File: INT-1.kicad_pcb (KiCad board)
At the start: 2 copper layers, 53 parts, among them SW1 SW_Push, U1 ATmega32U2-MU, U2 PRTR5V0U2X, Y1 Crystal_GND24_Small

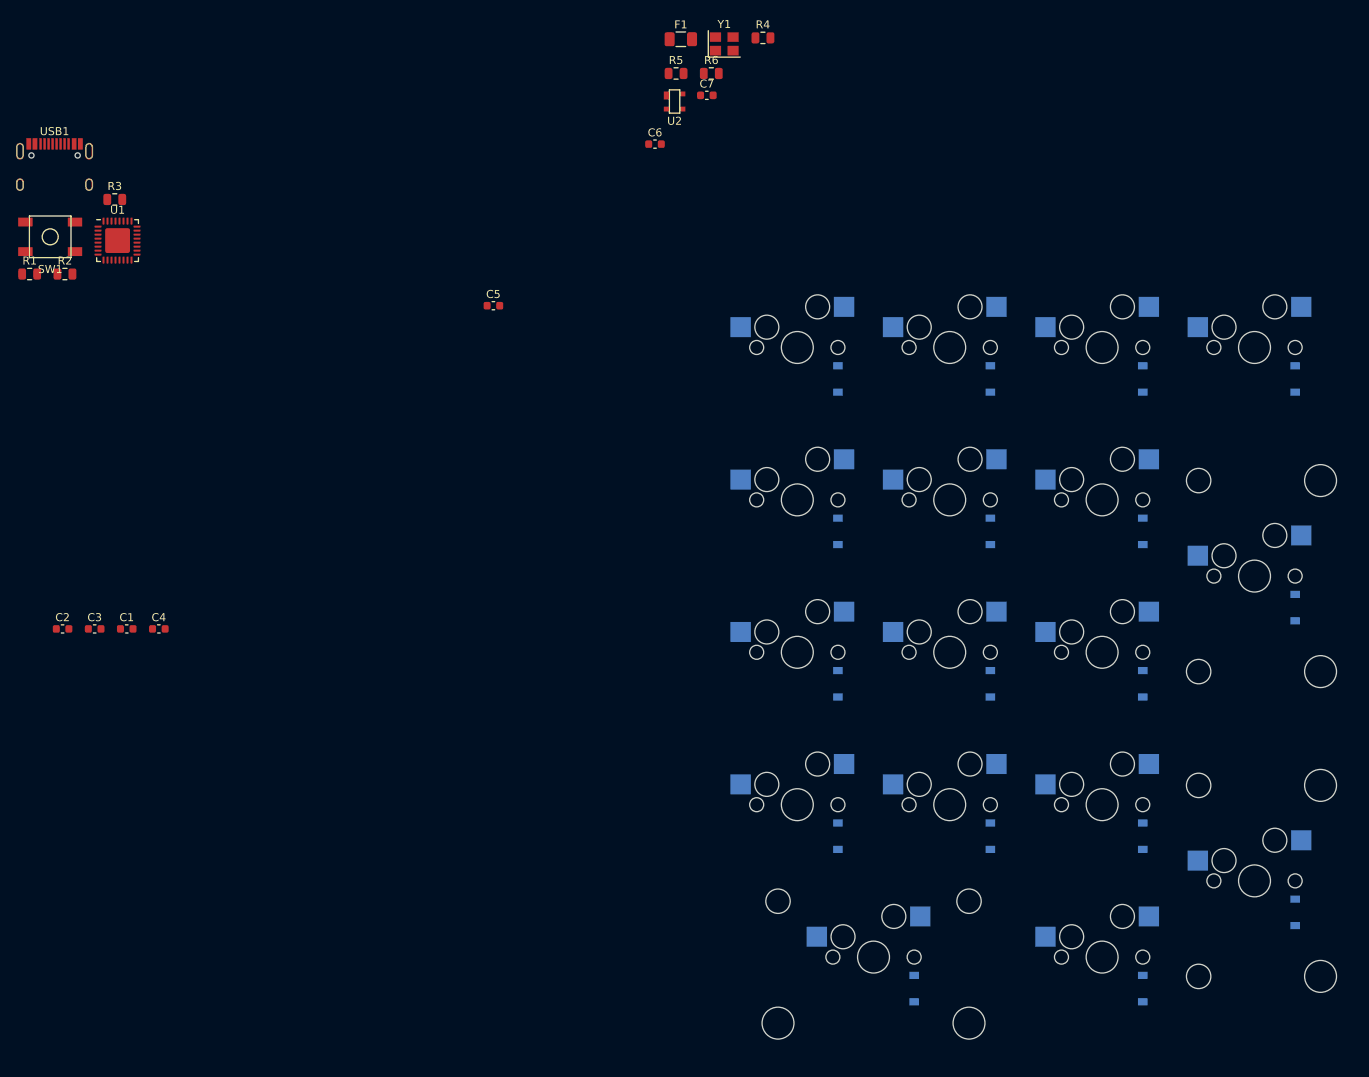
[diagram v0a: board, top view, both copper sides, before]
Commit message: Finished edge cuts
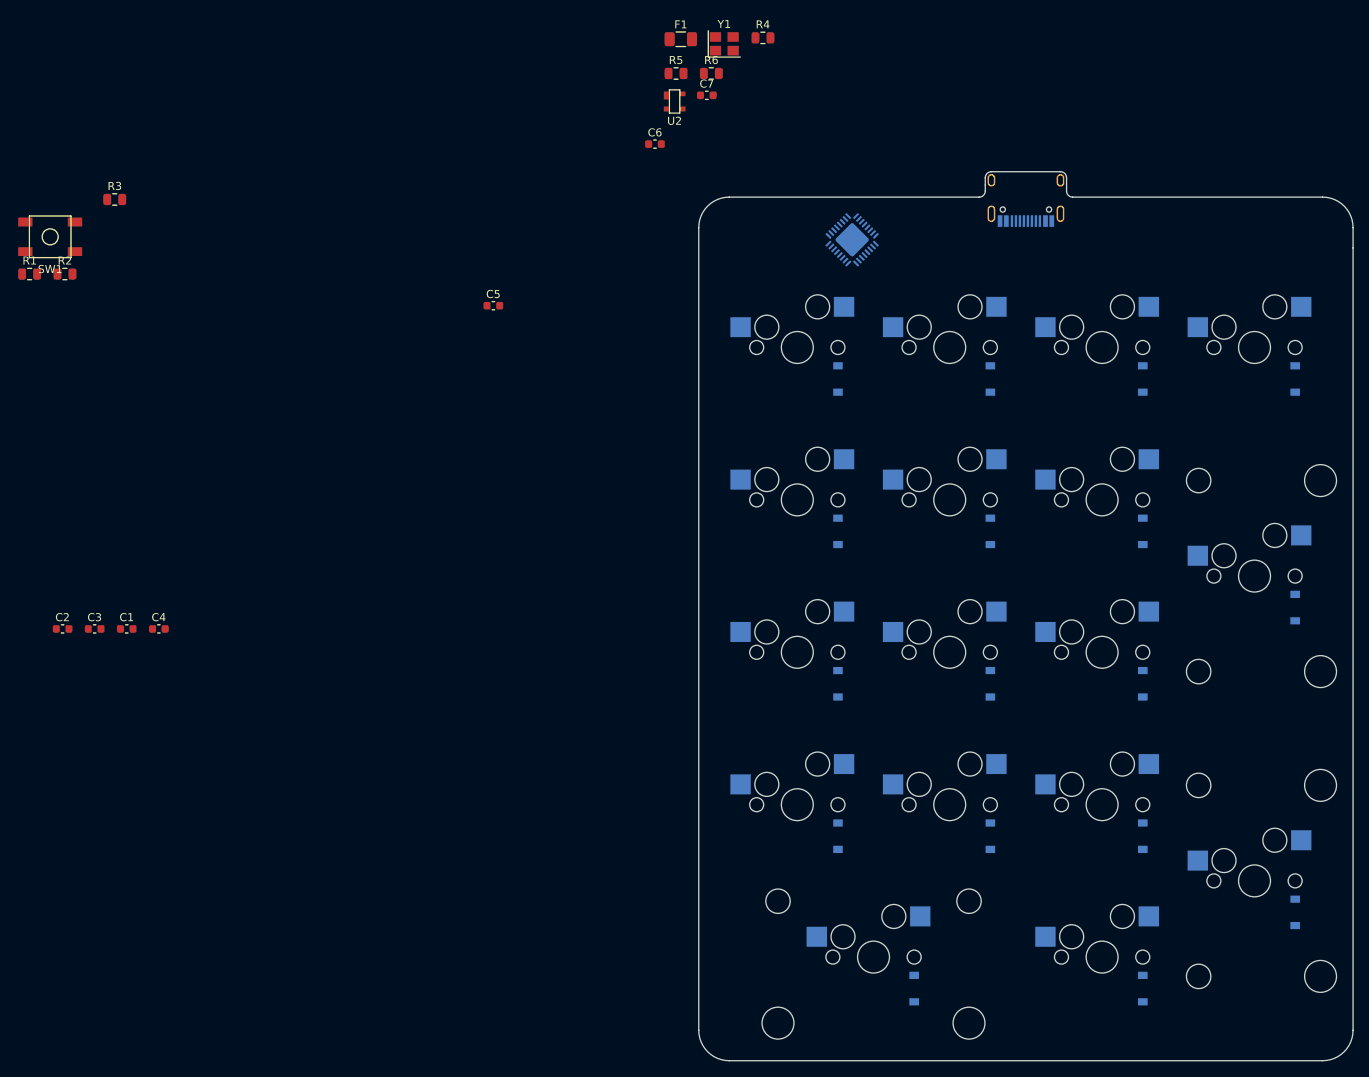
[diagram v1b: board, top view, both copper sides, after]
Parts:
- U1, USB1: moved to B.Cu
- moved USB1 121.6 mm to (152.1, 33.4)
- moved U1 91.8 mm to (130.4, 43.4), turned to 135 degrees
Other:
- board outline added: 81.8 x 111.1 mm

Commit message: Finished trace routing
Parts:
- removed C7: 0.1uF, Capacitor_SMD:C_0603_1608Metric
- C1, C2, C3, C5, C6, F1, R1, R2, R3, R4, R5, R6, SW1, U2, Y1: moved to B.Cu
- C4: value 10uF -> 4.7uF; moved to B.Cu
- moved C4 130.1 mm to (165.2, 45.5)
- moved C2 117.2 mm to (140.5, 48.4)
- moved R3 113.2 mm to (151.1, 47.5), turned to 90 degrees
- moved C1 113.1 mm to (140.6, 40.8), turned to 180 degrees
- moved C3 108.9 mm to (130.9, 39.1)
- moved R2 102.1 mm to (134.1, 48.8), turned to 180 degrees
- moved R1 100.6 mm to (127.9, 40.2), turned to 270 degrees
- moved SW1 91.0 mm to (121.2, 42.7), turned to 270 degrees
- moved C5 80.2 mm to (165.2, 42.5)
- moved C6 60.0 mm to (165.2, 39.6)
- moved F1 56.8 mm to (159.8, 43.8), turned to 90 degrees
- moved R6 48.1 mm to (155.7, 44.5), turned to 90 degrees
- moved U2 47.4 mm to (152.1, 44.1), turned to 180 degrees
- moved R5 45.6 mm to (148.6, 44.3), turned to 90 degrees
- moved R4 44.8 mm to (153.2, 47.5), turned to 90 degrees
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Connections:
- U1 pad 14: COL0 -> Net-(U1-Pad14)
- U1 pad 15: COL1 -> COL3
- U1 pad 16: COL2 -> ROW0
- U1 pad 17: COL3 -> ROW1
- U1 pad 18: ROW0 -> ROW2
- U1 pad 19: ROW1 -> COL2
- U1 pad 20: ROW2 -> COL1
- U1 pad 21: ROW3 -> COL0
- U1 pad 22: Net-(U1-Pad22) -> ROW3
- U1 pad 23: Net-(U1-Pad23) -> ROW4
- U1 pad 5: ROW4 -> Net-(U1-Pad5)
- U2 pad 2: Net-(R3-Pad2) -> Net-(R4-Pad2)
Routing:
- net COL2: track 0.00 -> 202.6 mm, vias 0 -> 5
- net ROW4: track 0.00 -> 185.7 mm
- net COL0: track 0.00 -> 166.5 mm, vias 0 -> 5
- net COL1: track 0.00 -> 164.1 mm, vias 0 -> 4
- net ROW3: track 0.00 -> 141.7 mm
- net ROW2: track 0.00 -> 141.3 mm
- net COL3: track 0.00 -> 129.2 mm, vias 0 -> 3
- net GND: track 0.00 -> 102.9 mm, vias 0 -> 2
- net ROW1: track 0.00 -> 98.5 mm
- net ROW0: track 0.00 -> 74.0 mm
- net +5V: track 0.00 -> 60.3 mm, vias 0 -> 4
- net D+: track 0.00 -> 37.4 mm, vias 0 -> 2
- net D-: track 0.00 -> 35.9 mm, vias 0 -> 2
- net VCC: track 0.00 -> 16.2 mm, vias 0 -> 3
- net Net-(R1-Pad2): track 0.00 -> 12.9 mm
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- added copper zone on B.Cu, net GND
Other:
- net class Power: trace_width 0.381 -> 0.25

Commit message: Added mounting holes
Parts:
- added REF**: Generic-Mounthole, random-keyboard-parts:Generic-Mounthole, F.Cu at (114.7, 142.9)
- added REF**: Generic-Mounthole, random-keyboard-parts:Generic-Mounthole, F.Cu at (189.5, 142.9)
- added REF**: Generic-Mounthole, random-keyboard-parts:Generic-Mounthole, F.Cu at (189.5, 41.3)
- added REF**: Generic-Mounthole, random-keyboard-parts:Generic-Mounthole, F.Cu at (114.7, 41.3)
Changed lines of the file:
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@@
     (tracks 442)
     (zones 0)
-    (modules 52)
+    (modules 56)
     (nets 54)
   )
@@
     (add_net VCC)
   )
+  (module random-keyboard-parts:Generic-Mounthole (layer F.Cu)
+    (at 114.681 142.875)
+    (attr virtual)
+    (fp_text reference REF** (at 0 2) (layer Dwgs.User)
+      (effects (font (size 1 1) (thickness 0.15)))
+    )
+    (fp_text value Generic-Mounthole (at 0 -2) (layer Dwgs.User)
+      (effects (font (size 1 1) (thickness 0.15)))
+    )
+    (pad 1 thru_hole circle (at 0 0) (size 3.5 3.5) (drill 2.2) (layers *.Cu *.Mask))
+  )
+  (module random-keyboard-parts:Generic-Mounthole (layer F.Cu)
+    (at 189.484 142.875)
+    (attr virtual)
+    (fp_text reference REF** (at 0 2) (layer Dwgs.User)
+      (effects (font (size 1 1) (thickness 0.15)))
+    )
+    (fp_text value Generic-Mounthole (at 0 -2) (layer Dwgs.User)
+      (effects (font (size 1 1) (thickness 0.15)))
+    )
+    (pad 1 thru_hole circle (at 0 0) (size 3.5 3.5) (drill 2.2) (layers *.Cu *.Mask))
+  )
+  (module random-keyboard-parts:Generic-Mounthole (layer F.Cu)
+    (at 189.484 41.275)
+    (attr virtual)
+    (fp_text reference REF** (at 0 2) (layer Dwgs.User)
+      (effects (font (size 1 1) (thickness 0.15)))
+    )
+    (fp_text value Generic-Mounthole (at 0 -2) (layer Dwgs.User)
+      (effects (font (size 1 1) (thickness 0.15)))
+    )
+    (pad 1 thru_hole circle (at 0 0) (size 3.5 3.5) (drill 2.2) (layers *.Cu *.Mask))
+  )
+  (module random-keyboard-parts:Generic-Mounthole (layer F.Cu)
+    (at 114.681 41.275)
+    (attr virtual)
+    (fp_text reference REF** (at 0 2) (layer Dwgs.User)
+      (effects (font (size 1 1) (thickness 0.15)))
+    )
+    (fp_text value Generic-Mounthole (at 0 -2) (layer Dwgs.User)
+      (effects (font (size 1 1) (thickness 0.15)))
+    )
+    (pad 1 thru_hole circle (at 0 0) (size 3.5 3.5) (drill 2.2) (layers *.Cu *.Mask))
+  )
   (module MX_Only:MXOnly-1U-Hotswap (layer F.Cu)

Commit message: Added Text
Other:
- board text added: "INT-1"
- board text added: "INT-1 Keypad PCB Rev 1.0 12/2/2022"
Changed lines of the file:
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@@
   (general
     (thickness 1.6)
-    (drawings 207)
+    (drawings 211)
     (tracks 442)
     (zones 0)
@@
     )
   )
+  (gr_text "INT-1 Keypad PCB Rev 1.0 12/2/2022" (at 167.132 144.399) (layer B.SilkS)
+    (effects (font (size 1 1) (thickness 0.15)) (justify mirror))
+  )
+  (gr_text "INT-1 Keypad PCB Rev 1.0 12/2/2022" (at 167.132 144.399) (layer F.SilkS)
+    (effects (font (size 1 1) (thickness 0.15)))
+  )
+  (gr_text INT-1 (at 172.466 43.18) (layer F.SilkS)
+    (effects (font (size 4.5 5) (thickness 0.3)))
+  )
+  (gr_text INT-1 (at 177.165 43.307) (layer B.SilkS)
+    (effects (font (size 3 3.5) (thickness 0.15)) (justify mirror))
+  )
   (gr_line (start 157.226 35.687) (end 157.226 36.576) (layer Edge.Cuts) (width 0.05))
